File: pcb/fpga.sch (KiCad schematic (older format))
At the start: 54 parts, among them J1 CONN_INTEGRALSTICK_FPGA_DEVICE, Q1 SSM6N58NU, Q2 SSM6N58NU, Q3 SSM6N58NU, U12 DSC6001HI2A-025.0000‎, U2 XC7A50T-1FTG256C, U9 AT24MAC402-UDFN

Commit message: Continued work on layout. Added some layer crossing caps. Initial power plane placement.
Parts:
- added C?: 0.47 uF, azonenberg_pcb:EIA_0402_CAP_NOSILK, symbol device:C
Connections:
- net 3V3: now also C?.2
- new net 1V0: C?.1
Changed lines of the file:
@@
 Sheet 6 8
 Title "INTEGRALSTICK Compute Module"
-Date "2018-11-14"
+Date "2018-11-19"
 Rev "0.1"
 Comp "Andrew D. Zonenberg"
@@
 Wire Wire Line
 	15050 8050 15600 8050
+$Comp
+L device:C C?
+U 1 1 5BFC76E4
+P 11200 7300
+AR Path="/5B6B7044/5BFC76E4" Ref="C?"  Part="1"
+AR Path="/5B6B702C/5BFC76E4" Ref="C?"  Part="1"
+F 0 "C?" H 11315 7346 50  0000 L CNN
+F 1 "0.47 uF" H 11315 7255 50  0000 L CNN
+F 2 "azonenberg_pcb:EIA_0402_CAP_NOSILK" H 11238 7150 50  0001 C CNN
+F 3 "" H 11200 7300 50  0001 C CNN
+	1    11200 7300
+	1    0    0    -1
+$EndComp
+Text HLabel 11100 7150 0    50   Input ~ 0
+1V0
+Text Label 11100 7450 2    50   ~ 0
+3V3
+Wire Wire Line
+	11100 7450 11200 7450
+Wire Wire Line
+	11200 7150 11100 7150
 $EndSCHEMATC

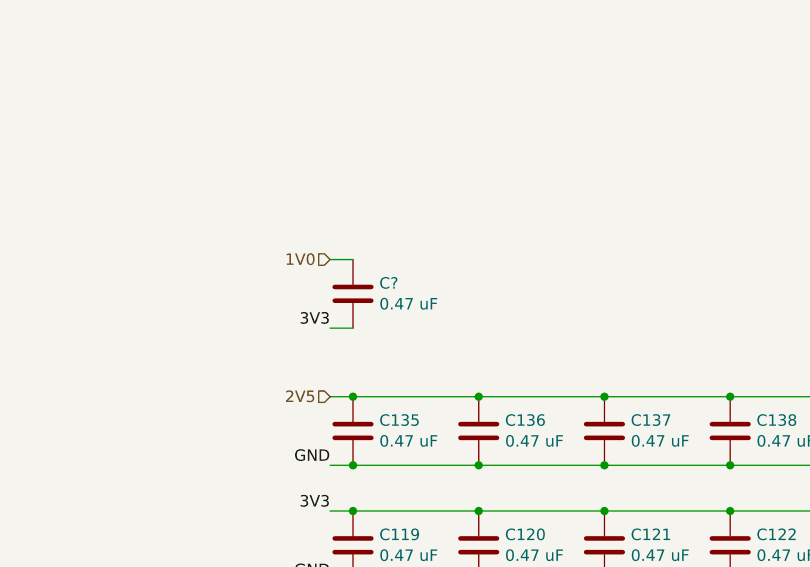
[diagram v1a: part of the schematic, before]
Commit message: Initial STM32 fanout
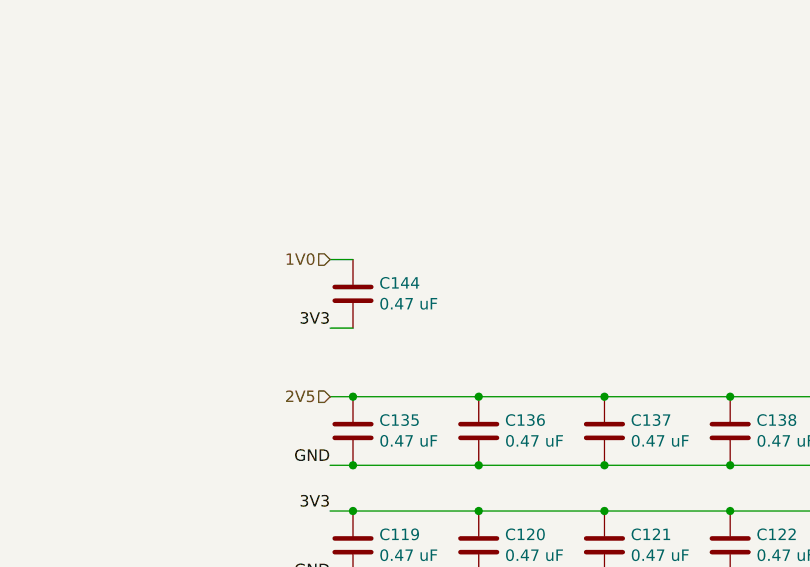
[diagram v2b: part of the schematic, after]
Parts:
- gave numbers to parts that had none: 1
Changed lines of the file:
@@
 Sheet 6 8
 Title "INTEGRALSTICK Compute Module"
-Date "2018-11-19"
+Date "2018-11-20"
 Rev "0.1"
 Comp "Andrew D. Zonenberg"
@@
 P 11200 7300
 AR Path="/5B6B7044/5BFC76E4" Ref="C?"  Part="1"
-AR Path="/5B6B702C/5BFC76E4" Ref="C?"  Part="1"
-F 0 "C?" H 11315 7346 50  0000 L CNN
+AR Path="/5B6B702C/5BFC76E4" Ref="C144"  Part="1"
+F 0 "C144" H 11315 7346 50  0000 L CNN
 F 1 "0.47 uF" H 11315 7255 50  0000 L CNN
 F 2 "azonenberg_pcb:EIA_0402_CAP_NOSILK" H 11238 7150 50  0001 C CNN

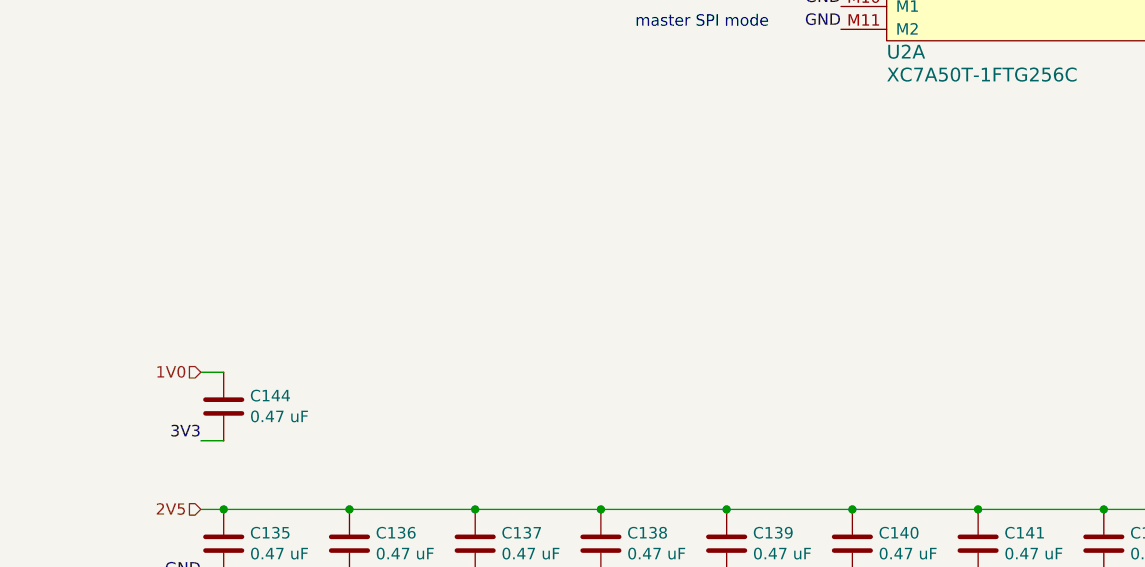
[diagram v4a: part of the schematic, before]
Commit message: Final PCB design being sent to fab for quotes
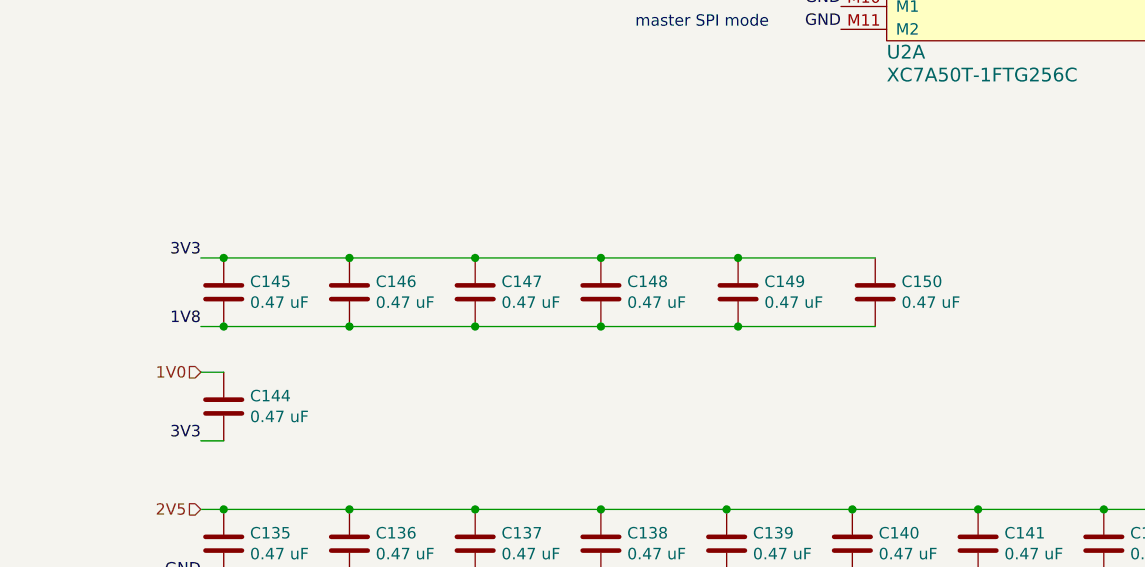
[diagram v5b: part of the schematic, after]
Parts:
- added C145, C146, C147, C148, C149, C150: 0.47 uF, azonenberg_pcb:EIA_0402_CAP_NOSILK, symbol device:C
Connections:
- net 1V8: now also C145.2, C146.2, C147.2, C148.2, C149.2, C150.2
- net 3V3: now also C145.1, C146.1, C147.1, C148.1, C149.1, C150.1
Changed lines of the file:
@@
 Sheet 6 8
 Title "INTEGRALSTICK Compute Module"
-Date "2018-11-29"
+Date "2018-12-02"
 Rev "0.1"
 Comp "Andrew D. Zonenberg"
@@
 Wire Wire Line
 	11200 7150 11100 7150
+$Comp
+L device:C C?
+U 1 1 5C06A03D
+P 11200 6800
+AR Path="/5B6B7044/5C06A03D" Ref="C?"  Part="1"
+AR Path="/5B6B702C/5C06A03D" Ref="C145"  Part="1"
+F 0 "C145" H 11315 6846 50  0000 L CNN
+F 1 "0.47 uF" H 11315 6755 50  0000 L CNN
+F 2 "azonenberg_pcb:EIA_0402_CAP_NOSILK" H 11238 6650 50  0001 C CNN
+F 3 "" H 11200 6800 50  0001 C CNN
+	1    11200 6800
+	1    0    0    -1
+$EndComp
+Text Label 11100 6650 2    50   ~ 0
+3V3
+Text Label 11100 6950 2    50   ~ 0
+1V8
+Wire Wire Line
+	11100 6950 11200 6950
+Wire Wire Line
+	11100 6650 11200 6650
+$Comp
+L device:C C?
+U 1 1 5C0711F3
+P 11750 6800
+AR Path="/5B6B7044/5C0711F3" Ref="C?"  Part="1"
+AR Path="/5B6B702C/5C0711F3" Ref="C146"  Part="1"
+F 0 "C146" H 11865 6846 50  0000 L CNN
+F 1 "0.47 uF" H 11865 6755 50  0000 L CNN
+F 2 "azonenberg_pcb:EIA_0402_CAP_NOSILK" H 11788 6650 50  0001 C CNN
+F 3 "" H 11750 6800 50  0001 C CNN
+	1    11750 6800
+	1    0    0    -1
+$EndComp
+Wire Wire Line
+	11750 6650 11200 6650
+Connection ~ 11200 6650
+Wire Wire Line
+	11200 6950 11750 6950
+Connection ~ 11200 6950
+$Comp
+L device:C C?
+U 1 1 5C078B6E
+P 12300 6800
+AR Path="/5B6B7044/5C078B6E" Ref="C?"  Part="1"
+AR Path="/5B6B702C/5C078B6E" Ref="C147"  Part="1"
+F 0 "C147" H 12415 6846 50  0000 L CNN
+F 1 "0.47 uF" H 12415 6755 50  0000 L CNN
+F 2 "azonenberg_pcb:EIA_0402_CAP_NOSILK" H 12338 6650 50  0001 C CNN
+F 3 "" H 12300 6800 50  0001 C CNN
+	1    12300 6800
+	1    0    0    -1
+$EndComp
+$Comp
+L device:C C?
+U 1 1 5C079069
+P 12850 6800
+AR Path="/5B6B7044/5C079069" Ref="C?"  Part="1"
+AR Path="/5B6B702C/5C079069" Ref="C148"  Part="1"
+F 0 "C148" H 12965 6846 50  0000 L CNN
+F 1 "0.47 uF" H 12965 6755 50  0000 L CNN
+F 2 "azonenberg_pcb:EIA_0402_CAP_NOSILK" H 12888 6650 50  0001 C CNN
+F 3 "" H 12850 6800 50  0001 C CNN
+	1    12850 6800
+	1    0    0    -1
+$EndComp
+Wire Wire Line
+	12850 6650 12300 6650
+Connection ~ 11750 6650
+Connection ~ 12300 6650
+Wire Wire Line
+	12300 6650 11750 6650
+Wire Wire Line
+	12850 6950 12300 6950
+Connection ~ 11750 6950
+Connection ~ 12300 6950
+Wire Wire Line
+	12300 6950 11750 6950
+$Comp
+L device:C C?
+U 1 1 5C08E6D3
+P 13450 6800
+AR Path="/5B6B7044/5C08E6D3" Ref="C?"  Part="1"
+AR Path="/5B6B702C/5C08E6D3" Ref="C149"  Part="1"
+F 0 "C149" H 13565 6846 50  0000 L CNN
+F 1 "0.47 uF" H 13565 6755 50  0000 L CNN
+F 2 "azonenberg_pcb:EIA_0402_CAP_NOSILK" H 13488 6650 50  0001 C CNN
+F 3 "" H 13450 6800 50  0001 C CNN
+	1    13450 6800
+	1    0    0    -1
+$EndComp
+Wire Wire Line
+	13450 6650 12850 6650
+Connection ~ 12850 6650
+Wire Wire Line
+	13450 6950 12850 6950
+Connection ~ 12850 6950
+$Comp
+L device:C C?
+U 1 1 5C09A189
+P 14050 6800
+AR Path="/5B6B7044/5C09A189" Ref="C?"  Part="1"
+AR Path="/5B6B702C/5C09A189" Ref="C150"  Part="1"
+F 0 "C150" H 14165 6846 50  0000 L CNN
+F 1 "0.47 uF" H 14165 6755 50  0000 L CNN
+F 2 "azonenberg_pcb:EIA_0402_CAP_NOSILK" H 14088 6650 50  0001 C CNN
+F 3 "" H 14050 6800 50  0001 C CNN
+	1    14050 6800
+	1    0    0    -1
+$EndComp
+Wire Wire Line
+	14050 6650 13450 6650
+Connection ~ 13450 6650
+Wire Wire Line
+	14050 6950 13450 6950
+Connection ~ 13450 6950
 $EndSCHEMATC

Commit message: Updated integralstick schematic to fix library paths. No content changes.
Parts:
- TP1: symbol conn:CONN_01X01 -> integralstick-rescue:CONN_01X01-conn
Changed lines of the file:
@@
 AR Path="/5B6B703A/5B8B40C5" Ref="J?"  Part="2"
 AR Path="/5B6B702C/5B8B40C5" Ref="J1"  Part="3"
+AR Path="/5B8B40C5" Ref="J1"  Part="3"
 F 0 "J1" H 1950 3450 50  0000 C CNN
 F 1 "CONN_INTEGRALSTICK_FPGA_DEVICE" H 1700 3550 50  0000 C CNN
@@
 AR Path="/5B6B703A/5BCD3CA2" Ref="J?"  Part="2"
 AR Path="/5B6B702C/5BCD3CA2" Ref="J1"  Part="4"
+AR Path="/5BCD3CA2" Ref="J1"  Part="4"
 F 0 "J1" H 6650 3950 50  0000 C CNN
 F 1 "CONN_INTEGRALSTICK_FPGA_DEVICE" H 6400 4050 50  0000 C CNN
@@
 	6850 7950 6850 8100
 $Comp
-L conn:CONN_01X01 TP1
+L integralstick-rescue:CONN_01X01-conn TP1
 U 1 1 5BF366F5
 P 8500 7750
